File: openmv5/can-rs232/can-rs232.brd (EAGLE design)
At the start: 35.6 x 26.7 mm, 61 parts, among them IC1 AP3032KTR-G1, IC2 AP3032KTR-G1, IC3 TCR2LF33,LM_CT, J1 OPENMV5-TOP, Q1 2N7002KW_R1_00001, U1 EKMB1307113K

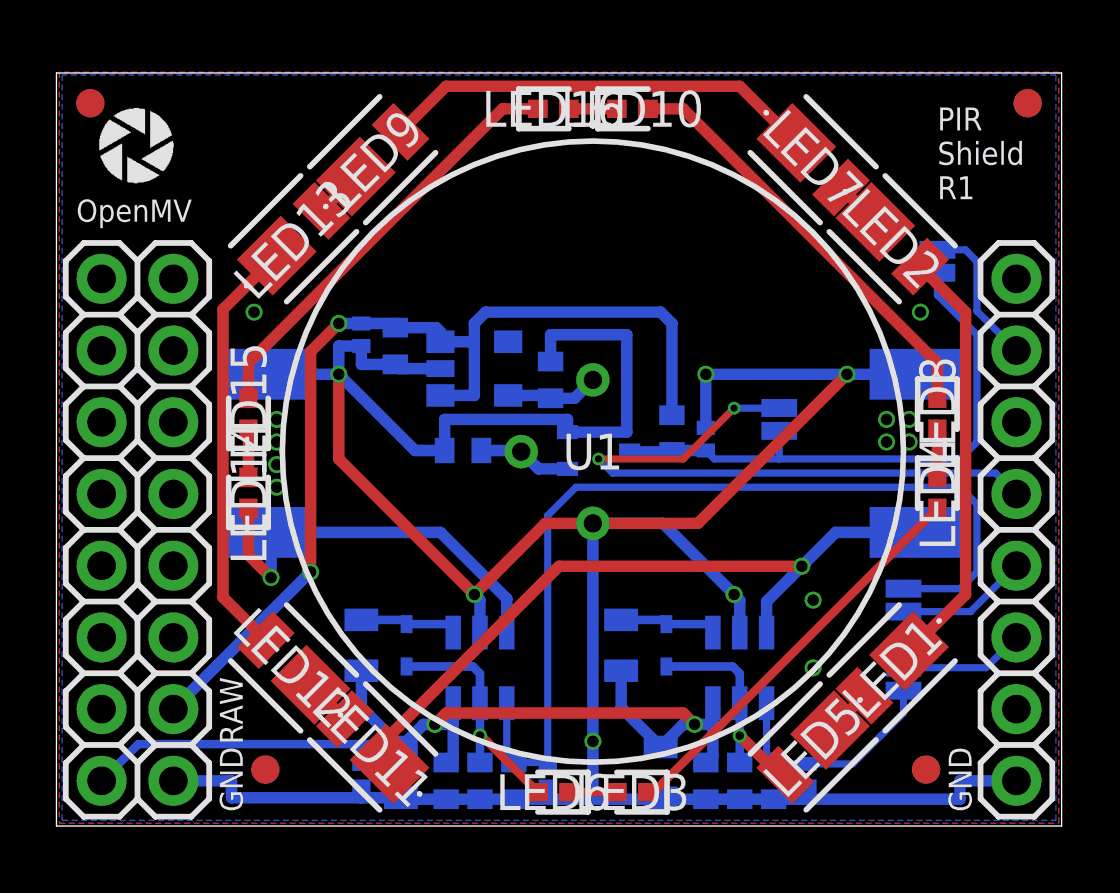
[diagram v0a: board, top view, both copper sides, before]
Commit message: Add CAN/RS232 shield
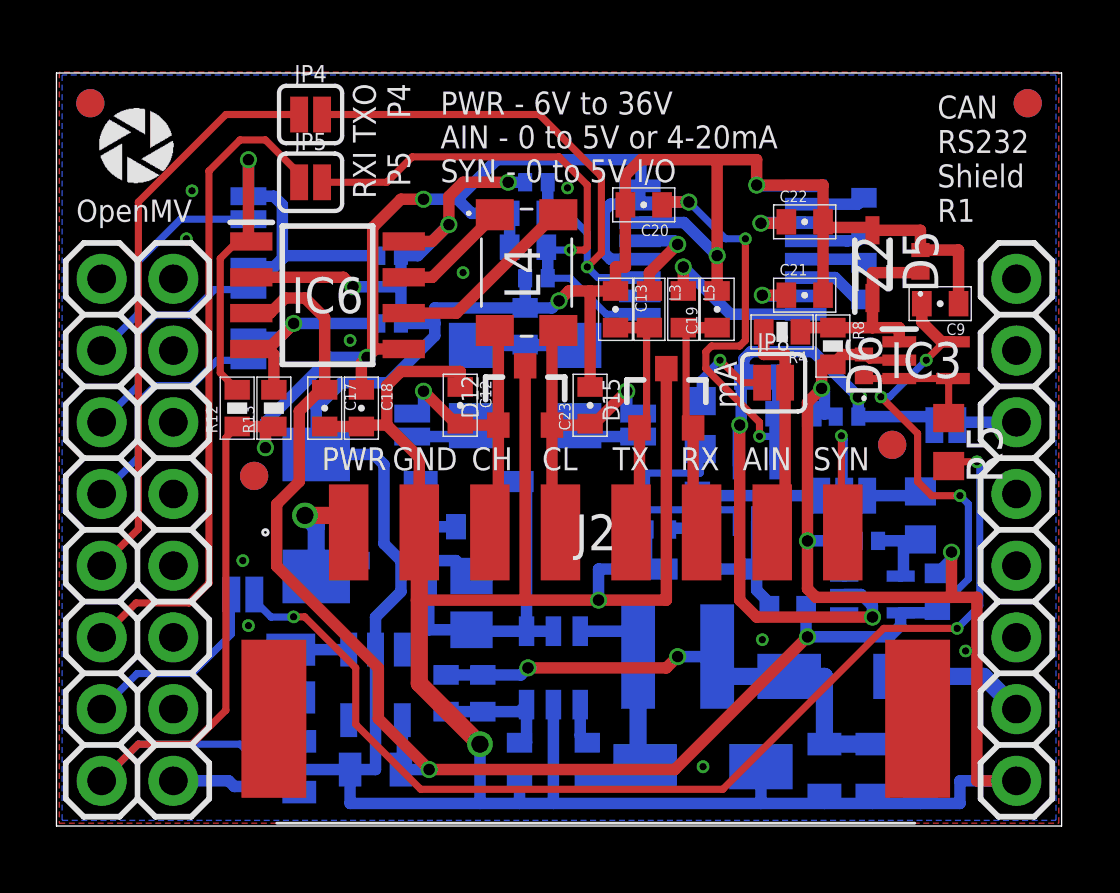
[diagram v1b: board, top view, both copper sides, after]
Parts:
- removed LED1, LED11, LED12, LED13, LED2, LED5, LED7, LED9: JB2835AWT-W-U57EA0000-N0000001, JB2835AWT-W-U57EA0000-N0000001:JB2835AWTWU57EA0000N0000001
- removed LED10, LED14, LED15, LED16, LED3, LED4, LED6, LED8: SFH_4053, SFH_4053:LEDC1005X55N
- added C10, C11, C14, C16, C17, C18, C20, C21, C22, C9: 0.1uF, sfe:0402-CAP
- added C12, C13, C19, C23: 100pF, sfe:0402-CAP
- added C15: 4.7nF, sfe:0402-CAP
- added D10, D11, D13, D14, D8, D9: CPDQT5V0HE-HF, CPDQT5V0HE-HF:CPDQT5V0HEHF
- added D12, D15: PESD1CAN, SparkFun-DiscreteSemi:SOT23-3
- added IC4: 74LVC1G07GW,125, 74LVC1G07GW_125:SOT65P212X110-5N
- added IC5: SN65C3221EPWR, SN65C3221EPWR:SOP65P640X120-16N
- added IC6: MCP2542FD-E_SN, MCP2542FD-E_SN:SOIC127P600X175-8N
- added J2: 1771088, 1771088:1771088
- added JP10, JP11, JP5, JP6, JP7: JUMPER-SMT_2_NC_PASTE_SILK, SparkFun-Jumpers:SMT-JUMPER_2_NC_PASTE_SILK
- added JP8: JUMPER-SMT_2_NO_SILK, SparkFun-Jumpers:SMT-JUMPER_2_NO_SILK
- added JP9: JUMPER-SMT_3_1-NC_PASTE_SILK, SparkFun-Jumpers:SMT-JUMPER_3_1-NC_PASTE_SILK
- added L3, L5: 100, sfe:C0402
- added L4: SRF4532-110Y, SRF4532-110Y:SRF4532101Y
- added R10, R12, R13, R14, R15: 10K, sfe:0402-RES
- added R11: 240, rcl:R0603
- added R16, R17: 60, rcl:R1206
- added R7, R8: 100K, sfe:0402-RES
- added R9: 470, rcl:R0603
- added Z1, Z3: MMSZ5231B-7-F, MMSZ5231B-7-F:SOD3716X145N
- added Z2: MM3Z3V6T1G, MM3Z3V6T1G:SOD2512X110N
- C1: value 22uF -> 0.1uF; device SparkFun-Capacitors:0805 -> sfe:0402-CAP
- C2: value 4.7uF -> 100pF
- C3, C6: value 1uF -> 22uF; device sfe:0402-CAP -> SparkFun-Capacitors:0805
- C5: value 4.7uF -> 10uF; device sfe:0402-CAP -> rcl:C0805
- C7, C8: value 4.7uF -> 22uF; device sfe:0402-CAP -> SparkFun-Capacitors:0805
- D1: value RB520S30T5G -> FM240A; device RB520S30T5G:SODFL1608X70N -> FM240A:DIOM5025X231N
- D2: value RB520S30T5G -> CPDQT5V0HE-HF; device RB520S30T5G:SODFL1608X70N -> CPDQT5V0HE-HF:CPDQT5V0HEHF
- D3: value CPDQT5V0HE-HF -> FM240A; device CPDQT5V0HE-HF:CPDQT5V0HEHF -> FM240A:DIOM5025X231N
- D4: value CPDQT5V0HE-HF -> SMAJ40CAE3_TR13; device CPDQT5V0HE-HF:CPDQT5V0HEHF -> SMAJ40CAe3_TR13:SMAJ40CAE3TR13
- IC1: value AP3032KTR-G1 -> TPS613222ADBVR; device AP3032KTR-G1:SOT95P280X145-6N -> TPS613222ADBVR:SOT95P280X145-5N
- IC2: value AP3032KTR-G1 -> AP64060WU-7; device AP3032KTR-G1:SOT95P280X145-6N -> AP64060WU-7:SOT95P280X100-6N
- IC3: value TCR2LF33,LM_CT -> LM321LVIDCKR; device TCR2LF33_LM_CT:TCR2LF33LMCT -> LM321LVIDCKR:SOT65P210X110-5N
- JP2: value JUMPER-SMT_2_NC_PASTE_SILK -> JUMPER-SMT_2_NO_SILK; device SparkFun-Jumpers:SMT-JUMPER_2_NC_PASTE_SILK -> SparkFun-Jumpers:SMT-JUMPER_2_NO_SILK
- JP4: value JUMPER-SMT_2_NO_SILK -> JUMPER-SMT_2_NC_PASTE_SILK; device SparkFun-Jumpers:SMT-JUMPER_2_NO_SILK -> SparkFun-Jumpers:SMT-JUMPER_2_NC_PASTE_SILK
- L1: value 6.8uH -> NRS4018T100MDGJ; device SparkFun-Coils:0805 -> NRS4018T100MDGJ:NRS4018T100MDGJ
- L2: value 6.8uH -> MAKK2016T2R2M; device SparkFun-Coils:0805 -> MAKK2016T2R2M:INDC2016X100N
- Q1: value 2N7002KW_R1_00001 -> SSM3J356R,LF; device 2N7002KW_R1_00001:SOT65P210X110-3N -> SSM3J356R_LF:SOTFL95P240X88-3N
- R1: value 100K -> 133K
- R2: value 3.9 -> 22.1K; device rcl:R2512 -> sfe:0402-RES
- R4: value 3.9 -> 51K; device rcl:R2512 -> sfe:0402-RES
- R5: value 100K -> 470; device sfe:0402-RES -> rcl:R0603
- U1: value EKMB1307113K -> 74LVC1G17SE-7; device EKMB1304111K:EKMB1304111K -> 74LVC1G17SE-7:SOT65P210X110-5N
- moved FD5 35.9 mm to (34.4, 25.6), flipped to the top
- moved FD7 33.2 mm to (1.20, 25.6), flipped to the top
- moved FD3 30.4 mm to (7.00, 12.4)
- moved JP1 28.6 mm to (6.80, 21.9), turned to 90 degrees
- moved D5 26.9 mm to (30.6, 20.0), flipped to the top, turned to 90 degrees
- moved JP2 25.8 mm to (6.80, 19.4)
- moved FD1 25.0 mm to (29.6, 13.5)
- moved JP3 24.6 mm to (6.80, 16.9), turned to 90 degrees
- moved C7 23.9 mm to (30.6, 2.00)
- moved FD6 23.9 mm to (34.4, 25.6)
- moved U$2 23.5 mm to (4.60, 21.2)
- moved U$1 22.4 mm to (35.0, 21.2)
- moved JP4 19.8 mm to (9.00, 25.2), flipped to the top, turned to 0 degrees
- moved R4 18.6 mm to (25.7, 17.5), flipped to the top, turned to 180 degrees
- moved C8 17.9 mm to (28.9, 2.00), turned to 90 degrees
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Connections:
- removed net I1: LED3.2, LED6.1
- removed net I2: LED3.1, LED4.2
- removed net I3: LED4.1, LED8.2
- removed net I4: LED10.2, LED8.1
- removed net I5: LED10.1, LED16.2
- removed net I6: LED15.2, LED16.1
- removed net I7: LED14.2, LED15.1
- removed net IFB: IC2.3, LED14.1, R4.2
- removed net IOV: C6.2, D2.1, IC2.5, LED6.2
- removed net ISW: D2.2, IC2.1, L2.2
- removed net OUT: Q1.1, R6.1, U1.2
- removed net P11_WAKEUP: D6.1, JP3.2, JP4.2, Q1.3, R5.1
- removed net P11_WAKEUP_INT: J1.15, JP3.1
- removed net P11_WAKEUP_INT_2: J1.13, JP4.1
- removed net P7_PWM: D3.1, IC1.4, JP1.2, R1.1
- removed net P7_PWM_INT: J1.11, JP1.1
- removed net P8_PWM: D4.1, IC2.4, JP2.2, R3.1
- removed net P8_PWM_INT: J1.12, JP2.1
- removed net RAW: C7.2, D7.1, IC3.1, IC3.3, J1.23, R5.2
- removed net VDD: C8.2, IC3.5, U1.1
- removed net W1: LED1.2, LED5.1
- removed net W2: LED1.1, LED2.2
- removed net W3: LED2.1, LED7.2
- removed net W4: LED7.1, LED9.2
- removed net W5: LED13.2, LED9.1
- removed net W6: LED12.2, LED13.1
- removed net W7: LED11.2, LED12.1
- removed net WFB: IC1.3, LED11.1, R2.2
- removed net WOV: C3.2, D1.1, IC1.5, LED5.2
- removed net WSW: D1.2, IC1.1, L1.2
- new net AIN: J2.7, JP8.2, R4.2
- new net AIN_INT: D5.1, IC3.1, R4.1, R8.1, Z2.1
- new net AIN_OUT: D6.1, IC3.3, IC3.4, R5.1
- new net AIN_S: JP8.1, R11.2
- new net C1+: C14.1, IC5.2
- new net C1-: C14.2, IC5.4
- new net C2+: C16.2, IC5.5
- new net C2-: C16.1, IC5.6
- new net CANH: C12.2, D12.1, J2.3, JP10.2, L4.2
- new net CANH_INT: IC6.7, L4.1
- new net CANH_J: JP10.1, R16.2
- new net CANL: C23.1, D12.2, J2.4, JP11.1, L4.3
- new net CANL_INT: IC6.6, L4.4
- new net CANL_J: JP11.2, R17.1
- new net CAN_RX: D11.1, IC6.4, JP3.2, R13.2
- new net CAN_RX_INT: J1.4, JP3.1
- new net CAN_S: C15.1, R16.1, R17.2
- new net CAN_TX: D10.1, IC6.1, JP1.2, JP2.2, R12.2
- new net CAN_TX_INT: J1.2, JP1.1
- new net CAN_TX_INT_2: J1.3, JP2.1
- new net EXT_RXI: C19.1, D15.2, J2.6, L5.2
- new net EXT_TXO: C13.2, D15.1, J2.5, L3.2
- new net EXT_VIN: D4.2, J2.1, Q1.3
- new net EXT_VIN_BST: C1.1, IC2.1
- new net EXT_VIN_FB: C2.2, IC2.3, R1.2, R2.1
- new net EXT_VIN_G: Q1.1, R3.1, Z1.2
- new net EXT_VIN_INT: C5.1, IC2.4, IC2.5, Q1.2, Z1.1
- new net EXT_VIN_OUT: C2.1, C6.2, C7.2, C8.2, D1.2, L1.2, R1.1
- new net EXT_VIN_SW: C1.2, D3.1, IC2.6, L1.1
- new net P10_FSYNC: D8.1, IC4.4, JP7.2, R7.2, U1.2
- new net P10_FSYNC_INT: J1.14, JP7.1
- new net P6_ADC: JP6.2, R5.2
- new net P6_ADC_INT: J1.7, JP6.1
- new net RS232_RXI: D14.1, IC5.9, JP5.2, R15.2
- new net RS232_RXI_INT: J1.6, JP5.1
- new net RS232_TXO: D13.1, IC5.11, JP4.2, R14.2
- new net RS232_TXO_INT: J1.5, JP4.1
- new net RXI: IC5.8, L5.1
- new net SW: IC1.1, L2.2
- new net SYNC: J2.8, JP9.2
- new net SYNC_IN: JP9.3, R10.2
- new net SYNC_IN_INT: D7.1, IC4.2, R10.1, R6.2, Z3.1
- new net SYNC_OUT: JP9.1, R9.2
- new net SYNC_OUT_INT: D9.1, R9.1, U1.4
- new net TXO: IC5.13, L3.1
- new net V+: C22.1, IC5.3
- new net V-: C21.1, IC5.7
- new net VIN: D1.1, J1.10
- new net V_BATT: C11.2, C17.1, C4.2, C9.2, IC1.4, IC3.5, IC6.3, R6.1, U1.5
- net GND: now also C10.1, C11.1, C12.1, C13.1, C15.2, C17.2, C18.2, C19.2, C20.2, C21.2, C22.2, C23.2, C5.2, C9.1, D10.2, D11.2, D12.3, D13.2, D14.2, D15.3, D2.2, D4.1, D8.2, D9.2, IC4.3, IC5.1, IC5.14, IC6.2, IC6.8, J2.2, R11.1, R2.2, R8.2, Z2.2, Z3.2; no longer C1.1, C2.1, C5.1, D4.2, Q1.2, R1.2, R2.1, R4.1, R6.2
- net VCC: now also C10.2, C18.1, C20.1, C3.2, D2.1, IC4.5, IC5.12, IC5.15, IC5.16, IC6.5, R12.1, R13.1, R14.1, R15.1, R7.1; no longer C1.2, C2.2, C4.2, C5.2, D5.1, IC1.6, IC2.6, L1.1
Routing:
- net GND: track 115.0 -> 222.2 mm, vias 18 -> 21
- net V_BATT: track 0.00 -> 61.8 mm, vias 0 -> 5
- net VCC: track 38.1 -> 77.9 mm, vias 2 -> 6
- net P6_ADC: track 0.00 -> 38.8 mm, vias 0 -> 3
- net RAW: track 36.2 -> 0.00 mm, vias 2 -> 0
- net P8_PWM: track 33.3 -> 0.00 mm
- net WFB: track 25.4 -> 0.00 mm, vias 1 -> 0
- net P10_FSYNC: track 0.00 -> 25.1 mm, vias 0 -> 3
- net RS232_RXI_INT: track 0.00 -> 23.6 mm
- net P11_WAKEUP_INT_2: track 22.5 -> 0.00 mm, vias 2 -> 0
- net RS232_TXO_INT: track 0.00 -> 20.4 mm
- net P11_WAKEUP: track 20.3 -> 0.00 mm
- net RS232_TXO: track 0.00 -> 20.3 mm, vias 0 -> 1
- net EXT_VIN_OUT: track 0.00 -> 20.2 mm, vias 0 -> 2
- net RS232_RXI: track 0.00 -> 18.8 mm, vias 0 -> 1
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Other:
- board text added: "4.7.23"
- board text added: "ADC P11"
- board text added: "AIN"
- board text added: "AIN - 0 to 5V or 4-20mA"
- board text added: "CAN RS232 Shield R1"
- board text added: "CAN/RS232 Shield R1"
- board text added: "CH"
- board text added: "CL"
- board text added: "CRX P3"
- board text added: "CTX P1"
- board text added: "CTX P2"
- board text added: "FSYNC P11"
- board text added: "I"
- board text added: "O"
- board text added: "PWR"
- board text added: "PWR - 6V to 36V"
- board text added: "RX"
- board text added: "RXI P5"
- board text added: "SYN"
- board text added: "SYN - 0 to 5V I/O"
- board text added: "TRM"
- board text added: "TX"
- board text added: "TXO P4"
- board text added: "VIN"
- board text added: "mA"
- board text removed: "3.31.23"
- board text removed: "Hot"
- board text removed: "IR"
- board text removed: "P7"
- board text removed: "P8"
- board text removed: "PIR Shield R1"
- board text removed: "WAKE P11"
- board text removed: "WAKE P9"
- board text removed: "WHITE"

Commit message: Fix drc issues
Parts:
- moved JP6 0.40 mm to (6.60, 8.60)
- moved FD3 0.28 mm to (6.80, 12.6)
- moved FD4 0.28 mm to (6.80, 12.6)
- moved FD1 0.10 mm to (29.5, 13.5)
- moved FD2 0.10 mm to (29.5, 13.5)
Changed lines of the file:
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@@
 <text x="10.5" y="23.9" size="0.8128" layer="21" font="vector" ratio="22" rot="R270">RXI
 P5</text>
-<text x="5.6" y="9.6" size="0.8128" layer="22" font="vector" ratio="22" rot="MR90">ADC
+<text x="5.6" y="9.9" size="0.8128" layer="22" font="vector" ratio="22" rot="MR90">ADC
 P11</text>
-<text x="29" y="13" size="0.8128" layer="22" font="vector" ratio="22" rot="MR0">O</text>
+<text x="28.9" y="13" size="0.8128" layer="22" font="vector" ratio="22" rot="MR0">O</text>
 <text x="27.3" y="13" size="0.8128" layer="22" font="vector" ratio="22" rot="MR0">I</text>
 <text x="24.1" y="14.8" size="0.8128" layer="21" font="vector" ratio="22" rot="R90">mA</text>
@@
 <element name="U$2" library="openmv" package="ROHS" value="" x="4.6" y="21.2" smashed="yes" rot="MR0"/>
 <element name="U$3" library="openmv" package="OMV-LOGO" value="" x="30.8" y="22.8" smashed="yes" rot="MR0"/>
-<element name="FD1" library="SparkFun-Aesthetics" library_urn="urn:adsk.eagle:library:507" package="FIDUCIAL-1X2" package3d_urn="urn:adsk.eagle:package:37108/1" value="FIDUCIAL1X2" x="29.6" y="13.5" smashed="yes"/>
-<element name="FD2" library="SparkFun-Aesthetics" library_urn="urn:adsk.eagle:library:507" package="FIDUCIAL-1X2" package3d_urn="urn:adsk.eagle:package:37108/1" value="FIDUCIAL1X2" x="29.6" y="13.5" smashed="yes" rot="MR0"/>
-<element name="FD4" library="SparkFun-Aesthetics" library_urn="urn:adsk.eagle:library:507" package="FIDUCIAL-1X2" package3d_urn="urn:adsk.eagle:package:37108/1" value="FIDUCIAL1X2" x="7" y="12.4" smashed="yes" rot="MR0"/>
-<element name="FD3" library="SparkFun-Aesthetics" library_urn="urn:adsk.eagle:library:507" package="FIDUCIAL-1X2" package3d_urn="urn:adsk.eagle:package:37108/1" value="FIDUCIAL1X2" x="7" y="12.4" smashed="yes"/>
+<element name="FD1" library="SparkFun-Aesthetics" library_urn="urn:adsk.eagle:library:507" package="FIDUCIAL-1X2" package3d_urn="urn:adsk.eagle:package:37108/1" value="FIDUCIAL1X2" x="29.5" y="13.5" smashed="yes"/>
+<element name="FD2" library="SparkFun-Aesthetics" library_urn="urn:adsk.eagle:library:507" package="FIDUCIAL-1X2" package3d_urn="urn:adsk.eagle:package:37108/1" value="FIDUCIAL1X2" x="29.5" y="13.5" smashed="yes" rot="MR0"/>
+<element name="FD4" library="SparkFun-Aesthetics" library_urn="urn:adsk.eagle:library:507" package="FIDUCIAL-1X2" package3d_urn="urn:adsk.eagle:package:37108/1" value="FIDUCIAL1X2" x="6.8" y="12.6" smashed="yes" rot="MR0"/>
+<element name="FD3" library="SparkFun-Aesthetics" library_urn="urn:adsk.eagle:library:507" package="FIDUCIAL-1X2" package3d_urn="urn:adsk.eagle:package:37108/1" value="FIDUCIAL1X2" x="6.8" y="12.6" smashed="yes"/>
 <element name="FD5" library="SparkFun-Aesthetics" library_urn="urn:adsk.eagle:library:507" package="FIDUCIAL-1X2" package3d_urn="urn:adsk.eagle:package:37108/1" value="FIDUCIAL1X2" x="34.4" y="25.6" smashed="yes"/>
 <element name="FD6" library="SparkFun-Aesthetics" library_urn="urn:adsk.eagle:library:507" package="FIDUCIAL-1X2" package3d_urn="urn:adsk.eagle:package:37108/1" value="FIDUCIAL1X2" x="34.4" y="25.6" smashed="yes" rot="MR0"/>
@@
 <attribute name="VALUE" x="5.657" y="19.4" size="0.6096" layer="28" font="vector" ratio="20" rot="MR90" align="top-center"/>
 </element>
-<element name="JP6" library="SparkFun-Jumpers" library_urn="urn:adsk.eagle:library:528" package="SMT-JUMPER_2_NC_PASTE_SILK" package3d_urn="urn:adsk.eagle:package:39282/1" value="JUMPER-SMT_2_NC_PASTE_SILK" x="6.6" y="8.2" smashed="yes" rot="MR180">
-<attribute name="NAME" x="6.6" y="7.057" size="0.6096" layer="26" font="vector" ratio="20" rot="MR180" align="bottom-center"/>
-<attribute name="VALUE" x="6.6" y="9.343" size="0.6096" layer="28" font="vector" ratio="20" rot="MR180" align="top-center"/>
+<element name="JP6" library="SparkFun-Jumpers" library_urn="urn:adsk.eagle:library:528" package="SMT-JUMPER_2_NC_PASTE_SILK" package3d_urn="urn:adsk.eagle:package:39282/1" value="JUMPER-SMT_2_NC_PASTE_SILK" x="6.6" y="8.6" smashed="yes" rot="MR180">
+<attribute name="NAME" x="6.6" y="7.457" size="0.6096" layer="26" font="vector" ratio="20" rot="MR180" align="bottom-center"/>
+<attribute name="VALUE" x="6.6" y="9.743" size="0.6096" layer="28" font="vector" ratio="20" rot="MR180" align="top-center"/>
 </element>
 <element name="R8" library="sfe" package="0402-RES" value="100K" x="27.5" y="17" smashed="yes" rot="R270">
@@
 <via x="18.1" y="22.6" extent="1-16" drill="0.254"/>
 <via x="10.4" y="17.2" extent="1-16" drill="0.254"/>
-<via x="6.6" y="9.4" extent="1-16" drill="0.254"/>
+<via x="6.6" y="11.3" extent="1-16" drill="0.254"/>
 <via x="6.8" y="7.1" extent="1-16" drill="0.254"/>
 <via x="4.6" y="20.8" extent="1-16" drill="0.254"/>
@@
 <contactref element="JP6" pad="1"/>
 <wire x1="1.6" y1="4.14" x2="2.86" y2="5.4" width="0.254" layer="16"/>
-<wire x1="6.1936" y1="6.7936" x2="6.1936" y2="8.2" width="0.254" layer="16"/>
+<wire x1="6.1936" y1="6.7936" x2="6.1936" y2="8.6" width="0.254" layer="16"/>
 <wire x1="2.86" y1="5.4" x2="4.8" y2="5.4" width="0.254" layer="16"/>
 <wire x1="4.8" y1="5.4" x2="6.1936" y2="6.7936" width="0.254" layer="16"/>
@@
 <contactref element="JP6" pad="2"/>
 <contactref element="R5" pad="2"/>
-<wire x1="7.0064" y1="8.2" x2="7.0064" y2="7.9936" width="0.254" layer="16"/>
+<wire x1="7.0064" y1="8.6" x2="7.0064" y2="7.9936" width="0.254" layer="16"/>
 <wire x1="7.6" y1="7.4" x2="8.4" y2="7.4" width="0.254" layer="16"/>
 <wire x1="8.4" y1="7.4" x2="8.4" y2="7.4074" width="0.254" layer="16"/>
@@
 <wire x1="31.9" y1="7" x2="32.7" y2="7.8" width="0.254" layer="16"/>
 <wire x1="23.6" y1="1.3" x2="29.3" y2="7" width="0.254" layer="1"/>
-<via x="32.6" y="12.9" extent="1-16" drill="0.254"/>
-<wire x1="32.6" y1="12.9" x2="31.75" y2="12.9" width="0.254" layer="1"/>
-<wire x1="31.75" y1="12.9" x2="31.6" y2="12.75" width="0.254" layer="1"/>
-<wire x1="32.7" y1="7.8" x2="32.7" y2="12.8" width="0.254" layer="16"/>
-<wire x1="32.7" y1="12.8" x2="32.6" y2="12.9" width="0.254" layer="16"/>
+<via x="32.6" y="12.7" extent="1-16" drill="0.254"/>
+<wire x1="32.6" y1="12.7" x2="31.65" y2="12.7" width="0.254" layer="1"/>
+<wire x1="31.6" y1="12.75" x2="31.65" y2="12.7" width="0.254" layer="1"/>
+<wire x1="32.7" y1="7.8" x2="32.7" y2="12.6" width="0.254" layer="16"/>
+<wire x1="32.7" y1="12.6" x2="32.6" y2="12.7" width="0.254" layer="16"/>
 </signal>
 <signal name="AIN" class="4">

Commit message: Add servo shield
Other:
- board text added: "ADC P6"
- board text added: "FSYNC P10"
- board text removed: "ADC P11"
- board text removed: "FSYNC P11"
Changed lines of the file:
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@@
 <text x="32.4" y="2.8" size="0.8128" layer="22" font="vector" ratio="22" rot="MR270">GND</text>
 <text x="28.5" y="17.5" size="0.8128" layer="22" font="vector" ratio="22" rot="MR180">FSYNC
-P11</text>
+P10</text>
 <text x="11.9" y="12.6" size="0.8128" layer="21" font="vector" ratio="22">GND</text>
 <text x="9.4" y="12.6" size="0.8128" layer="21" font="vector" ratio="22">PWR</text>
@@
 P5</text>
 <text x="5.6" y="9.9" size="0.8128" layer="22" font="vector" ratio="22" rot="MR90">ADC
-P11</text>
+P6</text>
 <text x="28.9" y="13" size="0.8128" layer="22" font="vector" ratio="22" rot="MR0">O</text>
 <text x="27.3" y="13" size="0.8128" layer="22" font="vector" ratio="22" rot="MR0">I</text>

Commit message: Remove zener diode from ADC circuit
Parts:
- Z2: value MM3Z3V6T1G -> DNP
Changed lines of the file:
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@@
 <attribute name="VALUE" x="29.695" y="14.235" size="1.27" layer="27" rot="R270"/>
 </element>
-<element name="Z2" library="MM3Z3V6T1G" package="SOD2512X110N" value="MM3Z3V6T1G" x="28.9" y="19.9" smashed="yes" rot="R90">
+<element name="Z2" library="MM3Z3V6T1G" package="SOD2512X110N" value="DNP" x="28.9" y="19.9" smashed="yes" rot="R90">
 <attribute name="DESCRIPTION" value="ON Semiconductor MM3Z3V6T1G Zener Diode, 3.6V 5% 200 mW SMT 2-Pin SOD-323" x="28.9" y="19.9" size="1.778" layer="27" rot="R90" display="off"/>
 <attribute name="HEIGHT" value="1.1mm" x="28.9" y="19.9" size="1.778" layer="27" rot="R90" display="off"/>
@@
 <attribute name="MPN" value="MM3Z3V6T1G" x="28.9" y="19.9" size="1.778" layer="27" rot="R90" display="off"/>
 <attribute name="NAME" x="28.9" y="19.9" size="1.27" layer="25" rot="R90" align="center"/>
+<attribute name="POPULATE" value="0" x="28.9" y="19.9" size="1.778" layer="27" rot="R90" display="off"/>
 <attribute name="VALUE" x="28.9" y="19.9" size="1.27" layer="27" rot="R90" align="center"/>
 </element>
